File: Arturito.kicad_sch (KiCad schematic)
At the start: 8 parts, among them IC1 L293D, J1 Alimentación, J2 Motor 1, J3 Motor 2, J4 Control_M1, J5 Control_M2

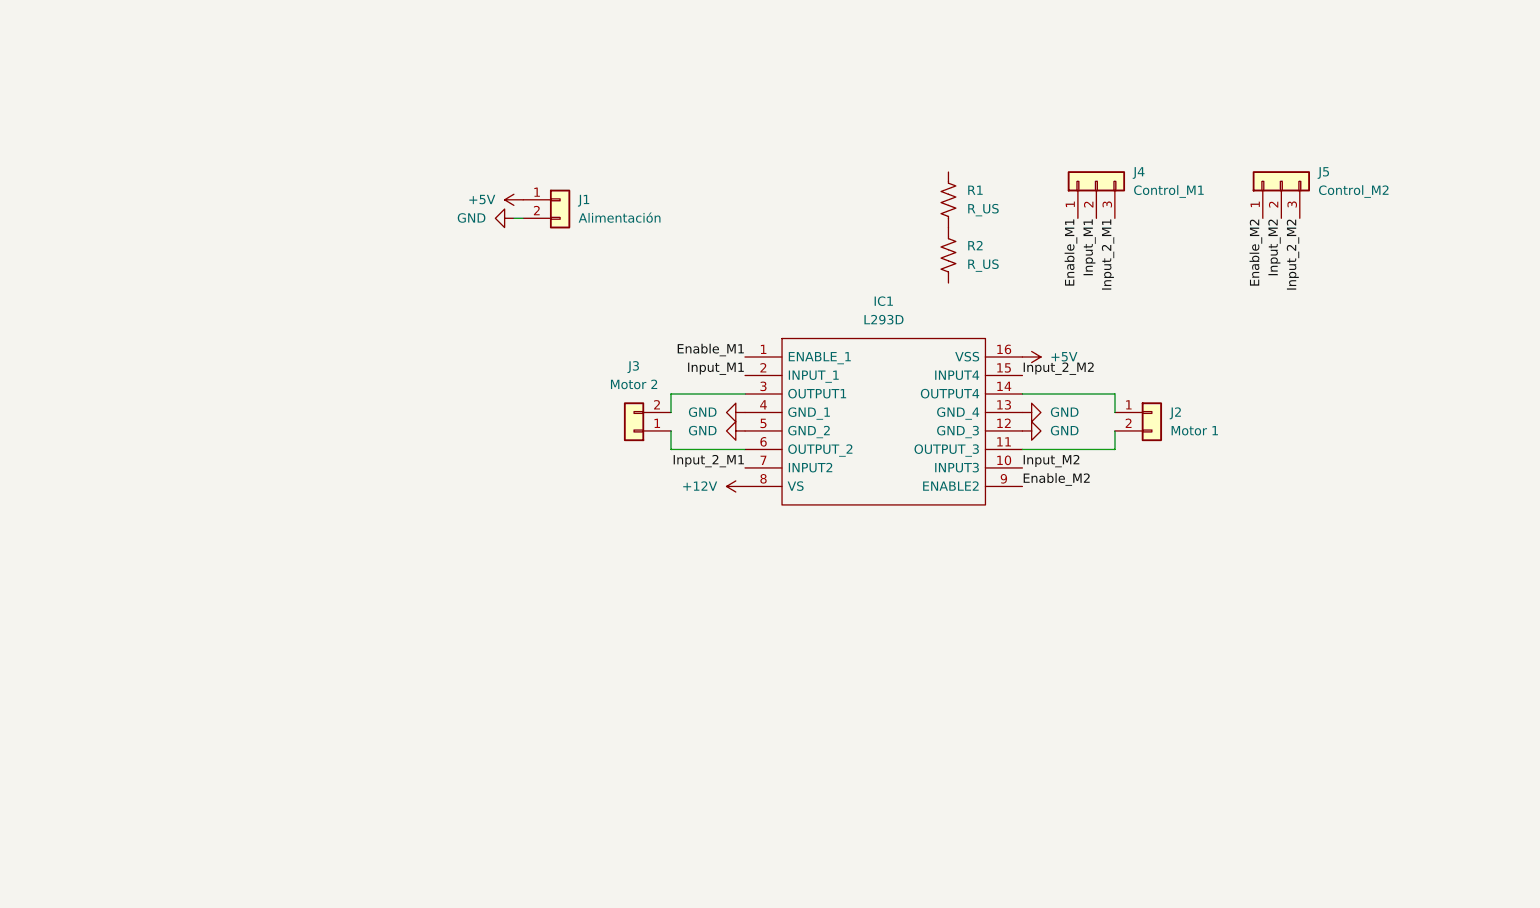
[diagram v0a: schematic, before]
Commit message: Actualizado con huellas y materiales extra al diagrama
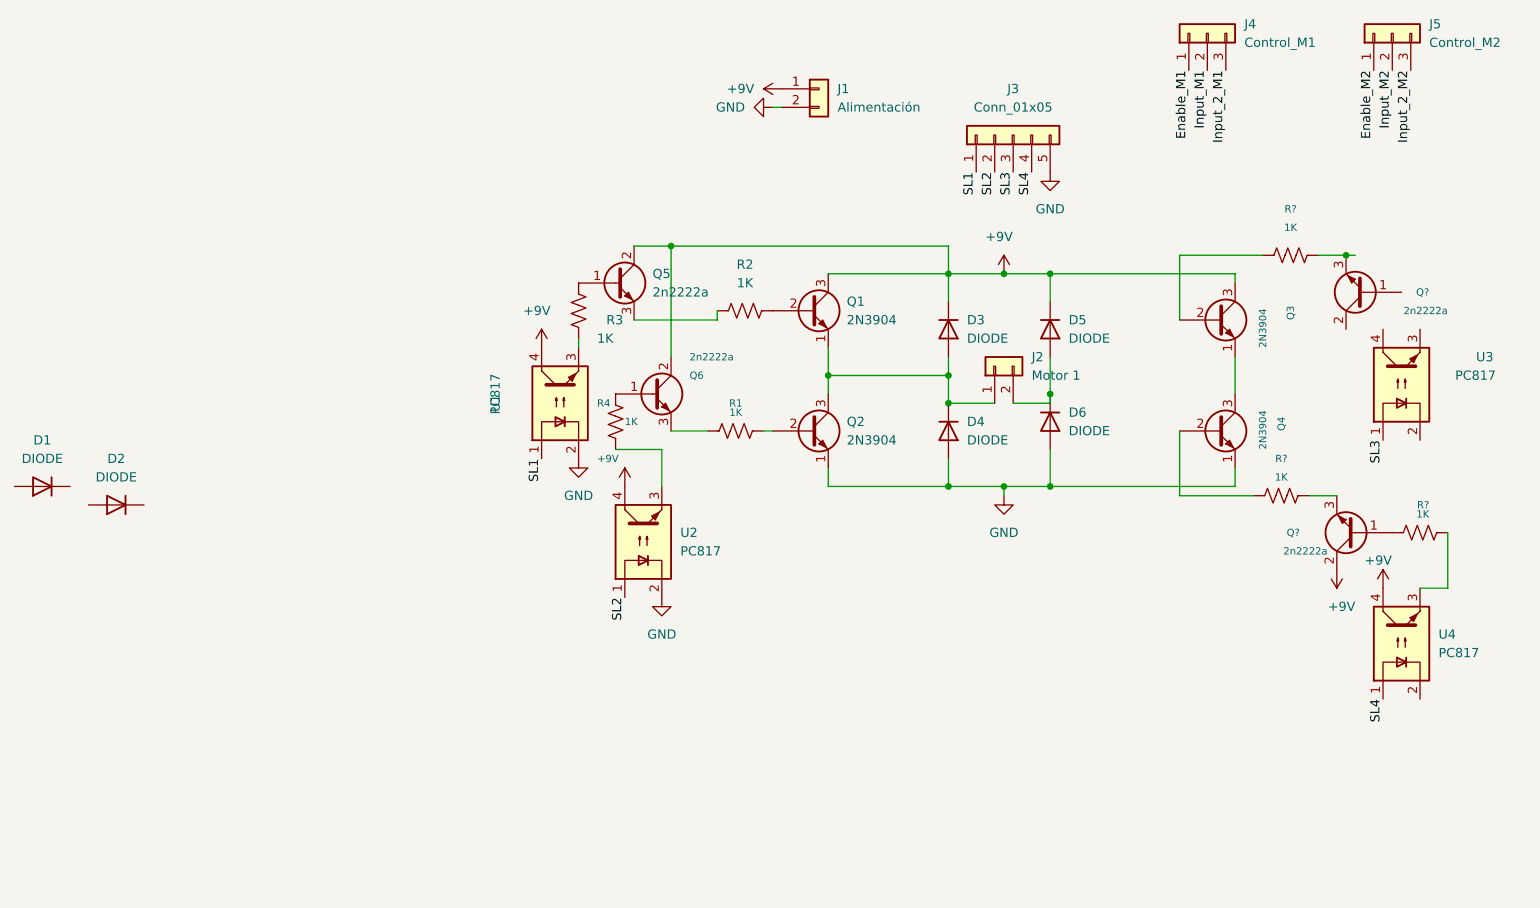
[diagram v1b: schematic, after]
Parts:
- removed IC1: L293D, Package_DIP:DIP-16_W7.62mm_Socket_LongPads, symbol L293D:L293D
- removed J3: Motor 2, TerminalBlock:TerminalBlock_bornier-2_P5.08mm, symbol Connector_Generic:Conn_01x02
- added D1, D2, D3, D4, D5, D6: DIODE, Diode_THT:D_5W_P12.70mm_Horizontal, symbol Simulation_SPICE:DIODE
- added J3: Conn_01x05, TerminalBlock:TerminalBlock_bornier-5_P5.08mm, symbol Connector_Generic:Conn_01x05
- added Q1, Q2, Q3, Q4: 2N3904, Package_TO_SOT_THT:TO-92_Inline, symbol Transistor_BJT:2N3904
- added Q5, Q6, Q? (x2): 2n2222a, Package_TO_SOT_THT:TO-92_Inline, symbol Transistor_BJT:2SD1047
- added R3, R4, R? (x3): 1K, Resistor_THT:R_Axial_DIN0309_L9.0mm_D3.2mm_P20.32mm_Horizontal, symbol Device:R_US
- added U1, U2, U3, U4: PC817, Package_DIP:DIP-4_W7.62mm, symbol Isolator:PC817
- R1, R2: value R_US -> 1K
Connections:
- net GND: now also D4.1 (A), D6.1 (A), J3.5 (Pin_5), Q2.1 (E), Q4.1 (E), U1.2, U2.2
- net at R2.1: now also Q5.3 (E); no longer R1.2
- net at R2.2: now also Q1.2 (B)
- net at J2.2 (Pin_2): now also D5.1 (A), D6.2 (K)
- net at J2.1 (Pin_1): now also D3.1 (A), D4.2 (K), Q1.1 (E), Q2.3 (C)
- net at R1.1: now also Q6.3 (E)
- net +5V renamed +9V
- net +9V: now also D3.2 (K), D5.2 (K), Q1.3 (C), Q3.3 (C), Q5.2 (C), Q6.2 (C), Q?.2 (C), U1.4, U2.4, U4.4
- new net: R?.1, U4.3
- new net: R3.1, U1.3
- new net: Q5.1 (B), R3.2
- new net: Q?.1 (B), R?.2
- new net: Q?.3 (E), R?.2 (x2)
- new net: R4.1, U2.3
- new net: Q2.2 (B), R1.2
- new net: Q4.2 (B), R?.1
- new net: Q3.1 (E), Q4.3 (C)
- new net: Q3.2 (B), R?.1
- new net: Q6.1 (B), R4.2
- new net SL1: J3.1 (Pin_1), U1.1
- new net SL2: J3.2 (Pin_2), U2.1
- new net SL3: J3.3 (Pin_3), U3.1
- new net SL4: J3.4 (Pin_4), U4.1
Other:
- moved on the sheet: J1, J4, J5, R1, R2

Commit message: Terminado DC,añadido stepper
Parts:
- removed D1, D2: DIODE, Diode_THT:D_5W_P12.70mm_Horizontal, symbol Simulation_SPICE:DIODE
- removed J4: Control_M1, TerminalBlock:TerminalBlock_bornier-2_P5.08mm, symbol Connector_Generic:Conn_01x03
- removed J5: Control_M2, TerminalBlock:TerminalBlock_bornier-2_P5.08mm, symbol Connector_Generic:Conn_01x03
- removed Q5, Q6, Q? (x2): 2n2222a, Package_TO_SOT_THT:TO-92_Inline, symbol Transistor_BJT:2SD1047
- removed R3, R4, R?: 1K, Resistor_THT:R_Axial_DIN0309_L9.0mm_D3.2mm_P20.32mm_Horizontal, symbol Device:R_US
- gave numbers to parts that had none: 2
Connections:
- net +9V: now also U3.4
- net GND: now also U3.2, U4.2
- net at U4.3: now also R3.2
- net at U1.3: now also R2.1
- net at U2.3: now also R1.1
- net at D5.1 (A), D6.2 (K), J2.2 (Pin_2): now also Q3.1 (E), Q4.3 (C)
- net at U3.3: now also R4.2
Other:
- moved on the sheet: D3, U1, U2, U3, U4

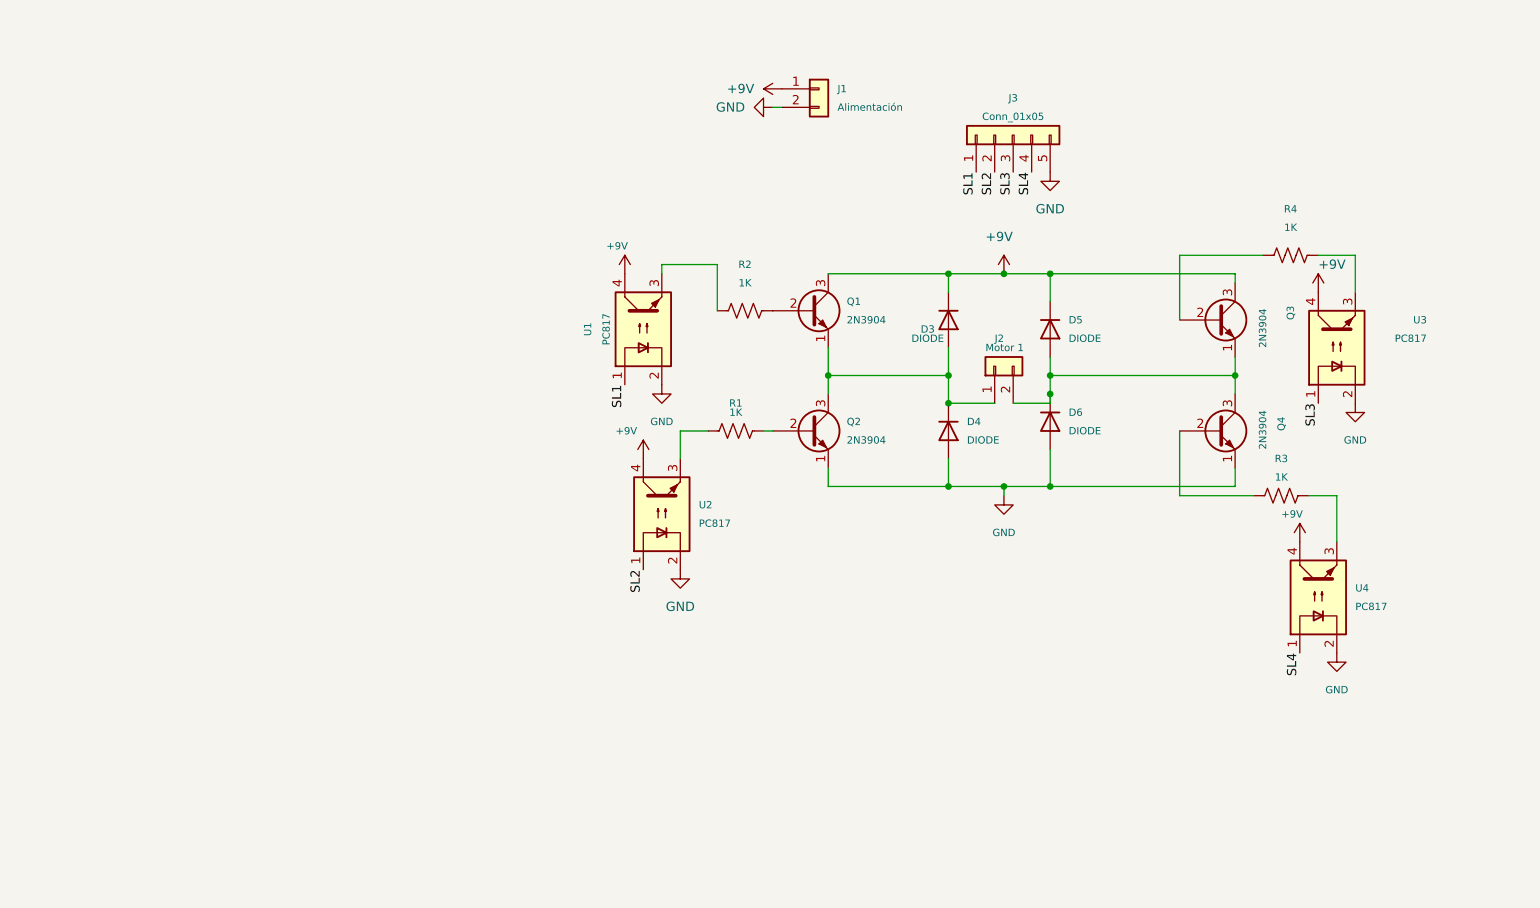
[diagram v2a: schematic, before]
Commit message: Redimensionado lo 3D y el control DC con relés
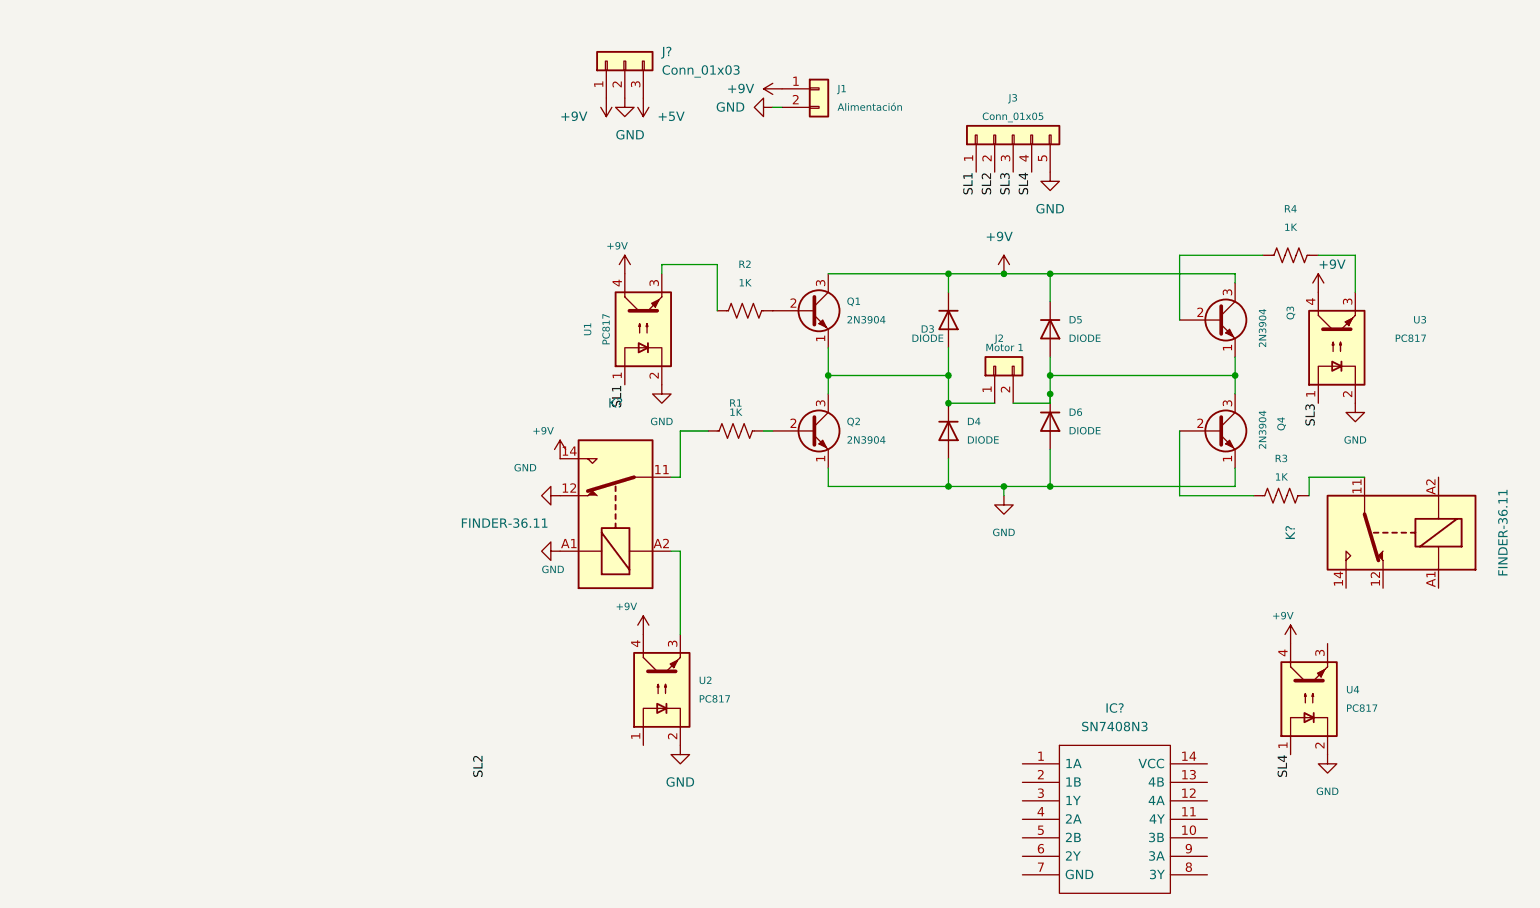
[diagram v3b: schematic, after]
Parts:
- added IC?: SN7408N3, DIP794W53P254L1930H508Q14N, symbol SN7408:SN7408N3
- added J?: Conn_01x03, symbol Connector_Generic:Conn_01x03
- added K? (x2): FINDER-36.11, Relay_THT:Relay_SPDT_Finder_36.11, symbol Relay:FINDER-36.11
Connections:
- net +9V: now also J?.1 (Pin_1), K?.14
- net GND: now also J?.2 (Pin_2), K?.12, K?.A1
- net SL2: no longer U2.1
- net at U4.3: no longer R3.2
- net at U2.3: now also K?.A2; no longer R1.1
- new net: K?.11, R3.2
- new net: K?.11, R1.1
- new net +5V: J?.3 (Pin_3)
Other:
- moved on the sheet: U2, U4

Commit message: Casi terminado
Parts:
- removed IC?: SN7408N3, DIP794W53P254L1930H508Q14N, symbol SN7408:SN7408N3
- removed K? (x2): FINDER-36.11, Relay_THT:Relay_SPDT_Finder_36.11, symbol Relay:FINDER-36.11
- J4: renamed from J?; footprint (none) -> TerminalBlock:TerminalBlock_bornier-3_P5.08mm
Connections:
- net SL2: now also U2.1
- net at U4.3: now also R3.2
- net at U2.3: now also R1.1
